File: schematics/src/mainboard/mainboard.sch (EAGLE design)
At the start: 64 parts, among them IC1 CEM3340, IC2 TL074P, IC4 TL074P, Q1 2N3904, Q2 2N3904

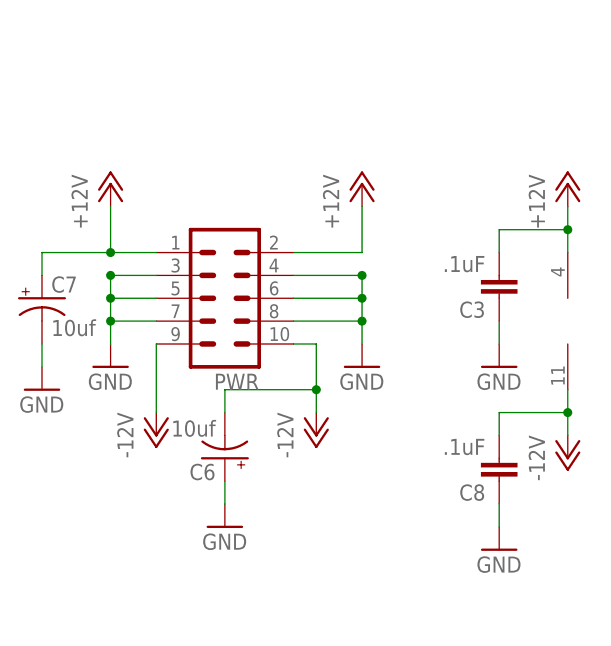
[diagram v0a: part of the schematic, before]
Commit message: Updated Schematics, Fixed Power Socket orientation
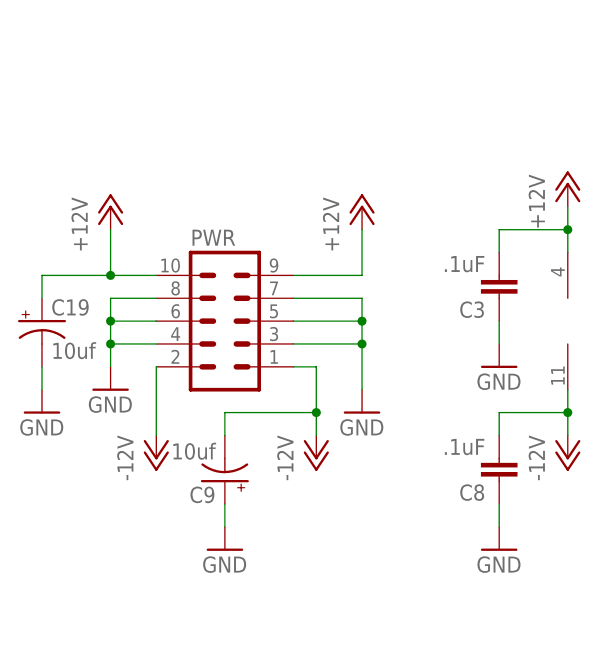
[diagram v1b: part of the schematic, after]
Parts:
- removed C6, C7: 10uf, resistor:CPOL-USE2.5-5
- added C19, C9: 10uf, resistor:CPOL-USE2.5-5
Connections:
- net +12V: now also C19.+, PWR.10, PWR.9; no longer C7.+, PWR.1, PWR.2
- net -12V: now also C9.-, PWR.1, PWR.2; no longer C6.-, PWR.10, PWR.9
- net GND: now also C19.-, C9.+; no longer C6.+, C7.-
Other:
- moved on the sheet: PWR
